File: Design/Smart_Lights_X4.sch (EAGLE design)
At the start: 64 parts, among them IC2 MP1584EN-LF-Z, J2 POWER_JACK, Q1 IRLR2905TRPBF, Q2 IRLR2905TRPBF, Q3 IRLR2905TRPBF, Q4 IRLR2905TRPBF, U1 ESP-32S

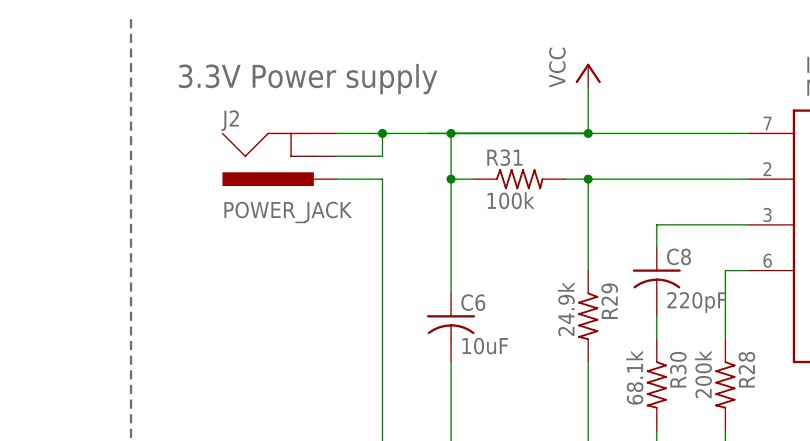
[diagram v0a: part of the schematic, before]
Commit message: Fixed DC Jack connection
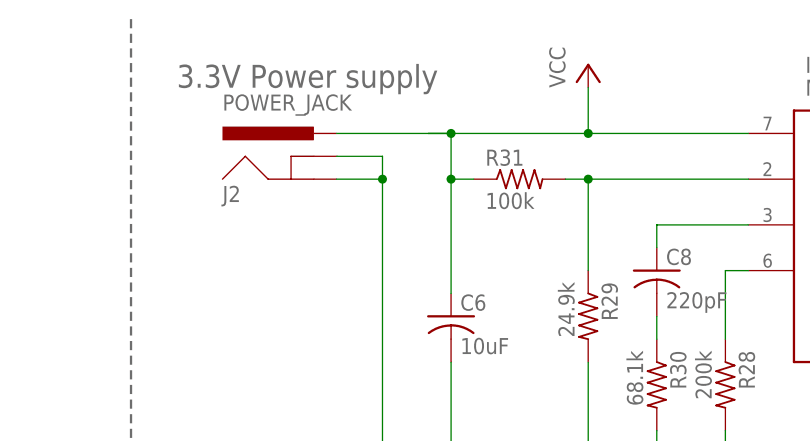
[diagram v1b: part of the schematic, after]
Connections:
- net GND: now also J2.GND, J2.GNDBREAK; no longer J2.PWR
- net VCC: now also J2.PWR; no longer J2.GND, J2.GNDBREAK
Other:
- moved on the sheet: J2
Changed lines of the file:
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@@
 <attribute name="VALUE" x="200.152" y="132.08" size="1.778" layer="96" font="vector" rot="R90" align="top-left"/>
 </instance>
-<instance part="J2" gate="G$1" x="109.22" y="165.1" smashed="yes" rot="MR180">
-<attribute name="VALUE" x="99.06" y="154.94" size="1.778" layer="96" font="vector" rot="MR180"/>
-<attribute name="NAME" x="99.06" y="165.1" size="1.778" layer="95" font="vector" rot="MR180"/>
+<instance part="J2" gate="G$1" x="109.22" y="154.94" smashed="yes">
+<attribute name="VALUE" x="99.06" y="165.1" size="1.778" layer="96" font="vector"/>
+<attribute name="NAME" x="99.06" y="154.94" size="1.778" layer="95" font="vector"/>
 </instance>
 <instance part="P+2" gate="VCC" x="139.7" y="170.18" smashed="yes">
@@
 </segment>
 <segment>
-<pinref part="J2" gate="G$1" pin="PWR"/>
 <pinref part="GND28" gate="1" pin="GND"/>
+<wire x1="116.84" y1="160.02" x2="116.84" y2="157.48" width="0.1524" layer="91"/>
+<pinref part="J2" gate="G$1" pin="GNDBREAK"/>
+<wire x1="116.84" y1="157.48" x2="116.84" y2="127" width="0.1524" layer="91"/>
+<wire x1="111.76" y1="160.02" x2="116.84" y2="160.02" width="0.1524" layer="91"/>
+<pinref part="J2" gate="G$1" pin="GND"/>
 <wire x1="111.76" y1="157.48" x2="116.84" y2="157.48" width="0.1524" layer="91"/>
-<wire x1="116.84" y1="157.48" x2="116.84" y2="127" width="0.1524" layer="91"/>
+<junction x="116.84" y="157.48"/>
 </segment>
 <segment>
@@
 <pinref part="IC2" gate="G$1" pin="VIN"/>
 <wire x1="157.48" y1="162.56" x2="139.7" y2="162.56" width="0.1524" layer="91"/>
-<wire x1="139.7" y1="162.56" x2="124.46" y2="162.56" width="0.1524" layer="91"/>
 <wire x1="124.46" y1="162.56" x2="124.46" y2="157.48" width="0.1524" layer="91"/>
 <junction x="124.46" y="157.48"/>
-<wire x1="139.7" y1="162.56" x2="124.46" y2="162.56" width="0.1524" layer="91"/>
 <junction x="139.7" y="162.56"/>
 <wire x1="124.46" y1="162.56" x2="121.92" y2="162.56" width="0.1524" layer="91"/>
-<wire x1="111.76" y1="160.02" x2="116.84" y2="160.02" width="0.1524" layer="91"/>
-<wire x1="116.84" y1="160.02" x2="116.84" y2="162.56" width="0.1524" layer="91"/>
-<wire x1="116.84" y1="162.56" x2="124.46" y2="162.56" width="0.1524" layer="91"/>
+<wire x1="111.76" y1="162.56" x2="124.46" y2="162.56" width="0.1524" layer="91"/>
 <wire x1="124.46" y1="162.56" x2="139.7" y2="162.56" width="0.1524" layer="91"/>
-<wire x1="111.76" y1="162.56" x2="116.84" y2="162.56" width="0.1524" layer="91"/>
-<junction x="116.84" y="162.56"/>
 <wire x1="139.7" y1="167.64" x2="139.7" y2="162.56" width="0.1524" layer="91"/>
-<pinref part="J2" gate="G$1" pin="GNDBREAK"/>
-<pinref part="J2" gate="G$1" pin="GND"/>
 <pinref part="P+2" gate="VCC" pin="VCC"/>
 <junction x="124.46" y="162.56"/>
-</segment>
-<segment>
+<pinref part="J2" gate="G$1" pin="PWR"/>
+</segment>
+<segment>

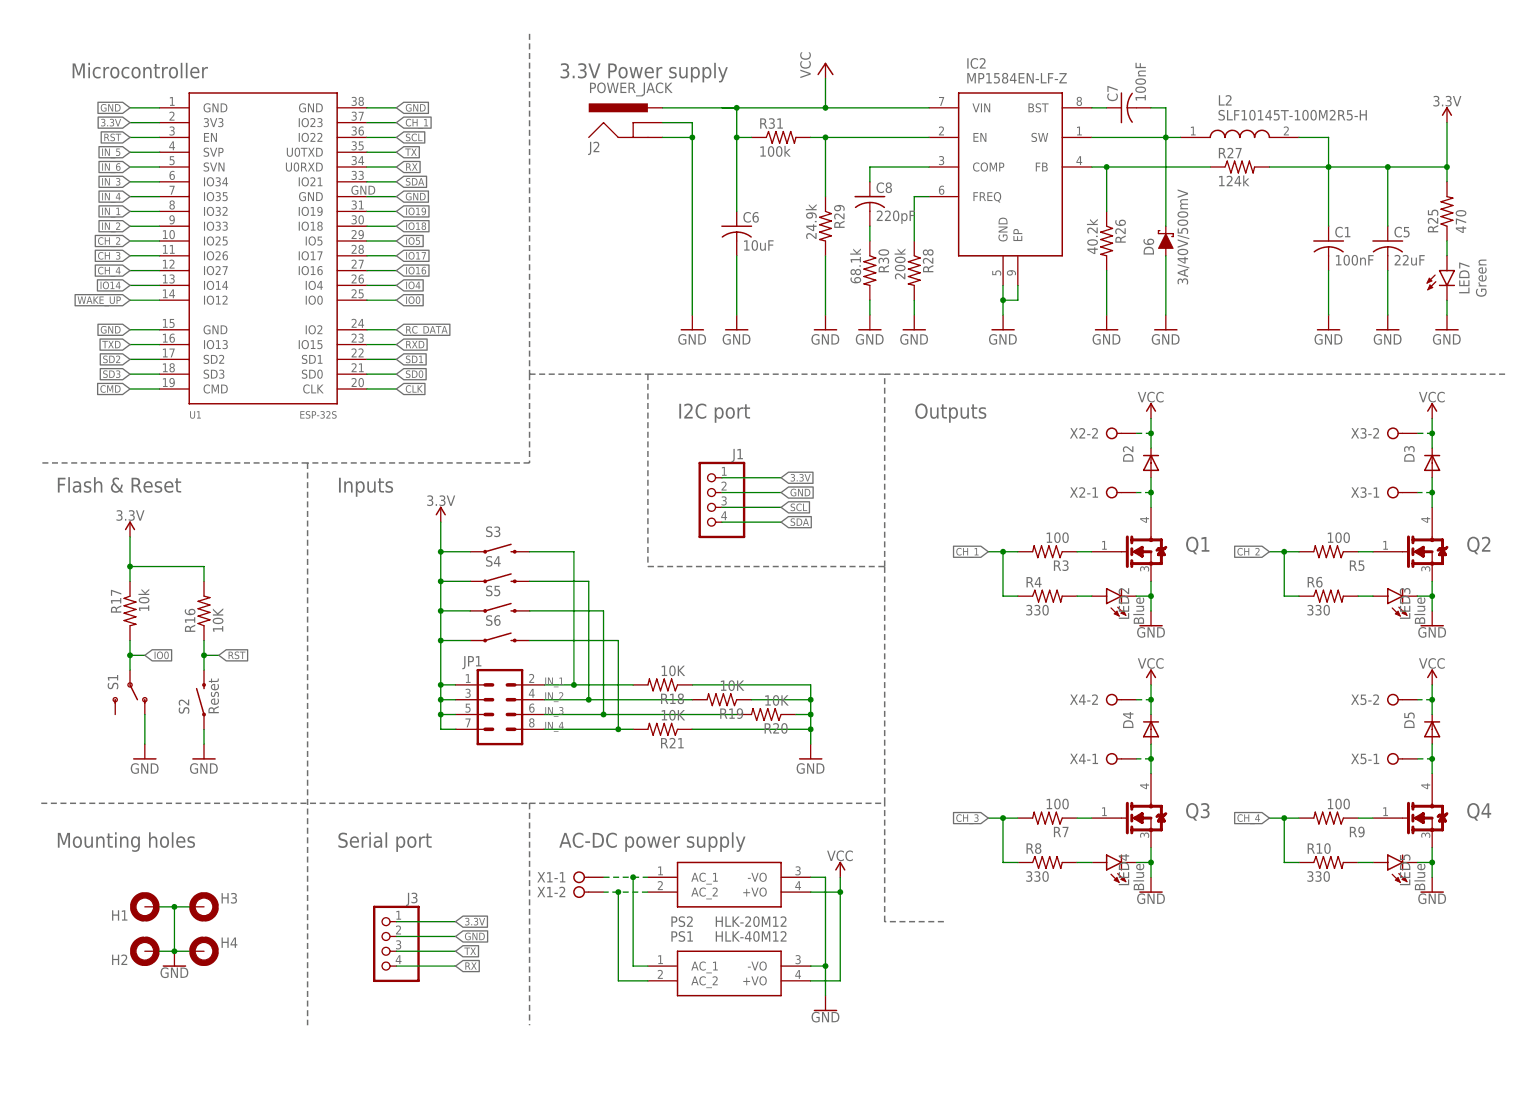
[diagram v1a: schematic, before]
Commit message: Resize dimensions to fit in the 92x87 enclosure
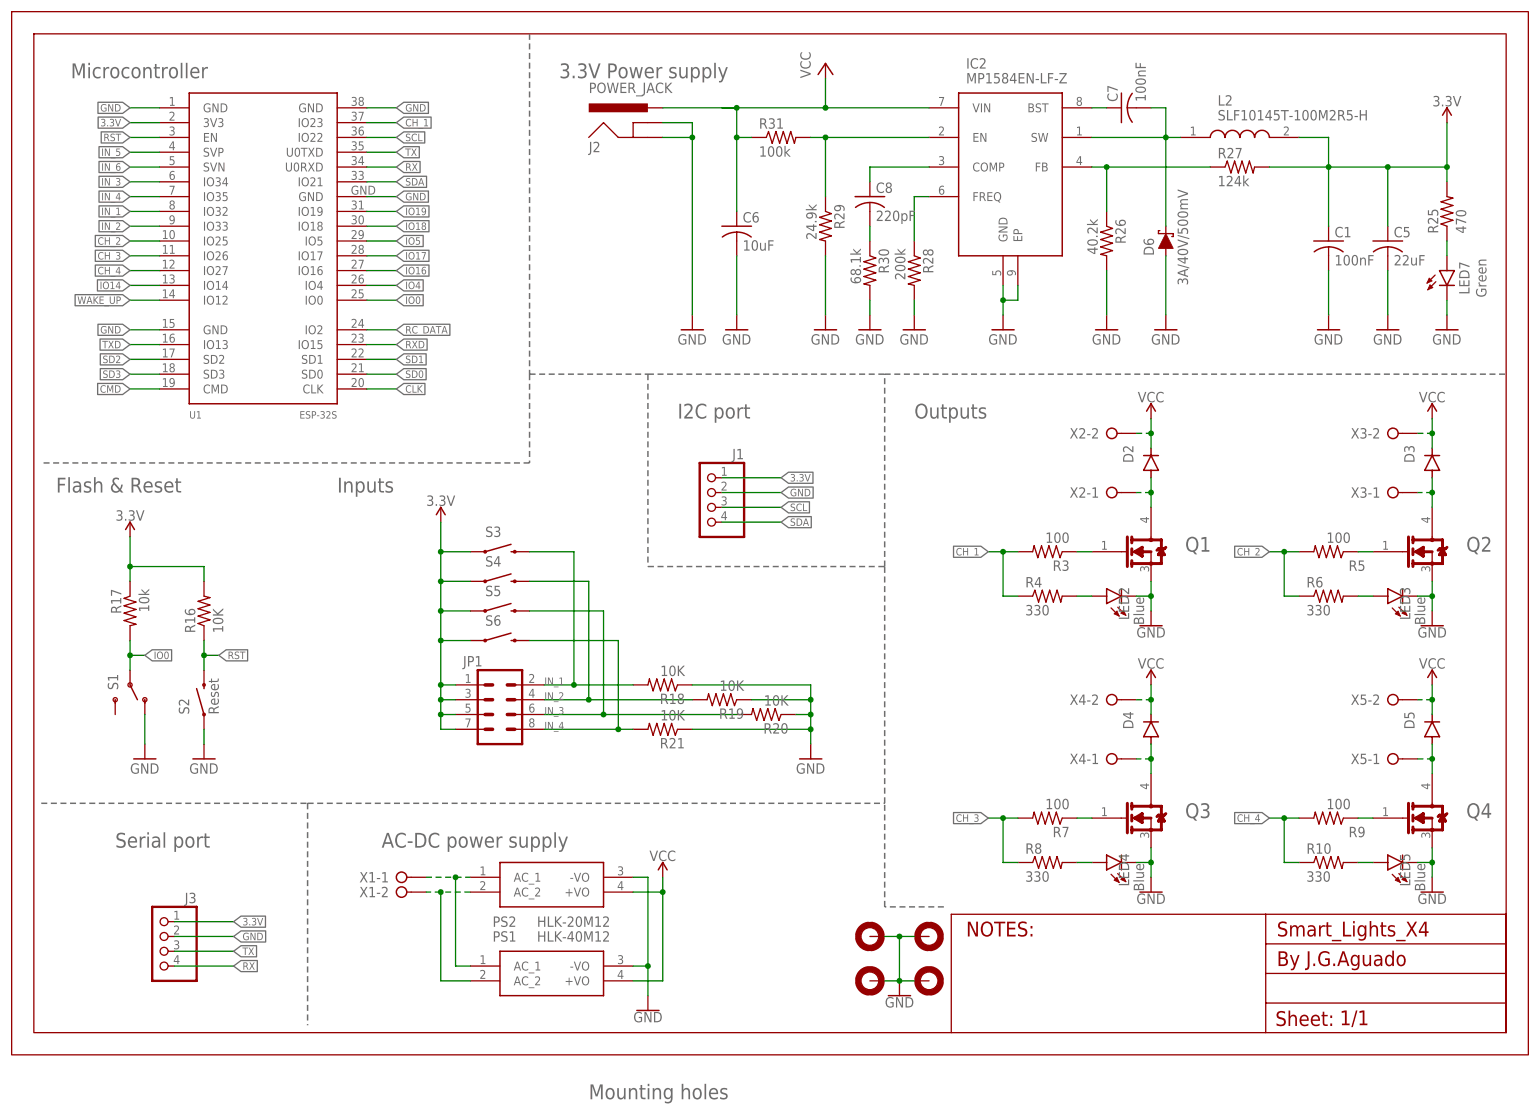
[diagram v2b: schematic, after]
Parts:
- removed H1, H2, H3, H4: MOUNT-PAD-ROUND, SpaceDIY_connectors:MOUNT-PAD-ROUND
- added FRAME1: (no value), SpaceDIY_symbols:A4L-LOC
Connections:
- net GND: now also FRAME1.MOUNT, FRAME1.MOUNT1, FRAME1.MOUNT2, FRAME1.MOUNT3; no longer H1.MOUNT, H2.MOUNT, H3.MOUNT, H4.MOUNT
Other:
- moved on the sheet: J3, PS1, PS2, X1-1, X1-2
